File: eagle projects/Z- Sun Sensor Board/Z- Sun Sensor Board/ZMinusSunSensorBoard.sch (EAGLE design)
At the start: 53 parts, among them U2 ADS7841E_2K5, U4 LM20BIM7X_NOPB, U6 TLV9051IDCKR, U8 TLV9051IDCKR, U9 TLV9051IDCKR

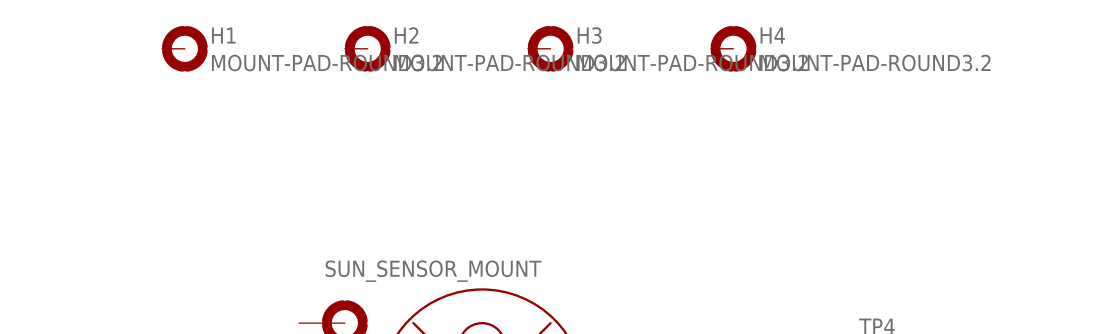
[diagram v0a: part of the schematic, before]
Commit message: Added mounting holes for sun sensor board, added standoff mounting holes to sensor board
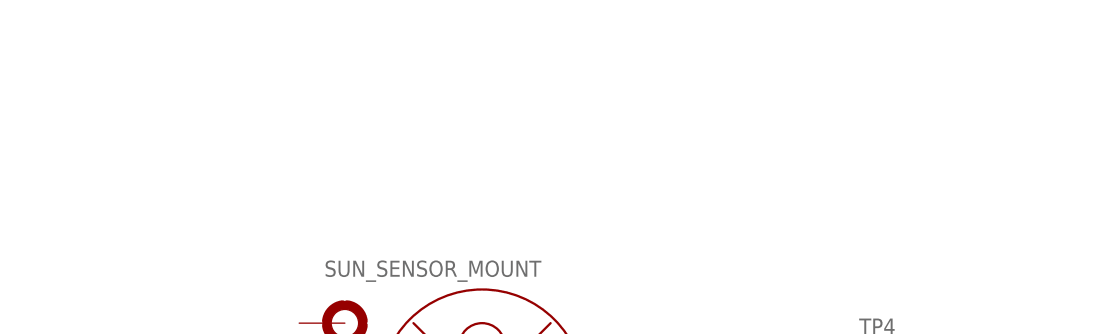
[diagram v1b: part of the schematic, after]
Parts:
- removed H1, H2, H3, H4: MOUNT-PAD-ROUND3.2, holes:MOUNT-PAD-ROUND3.2
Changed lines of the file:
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@@
 <part name="SUPPLY1" library="supply2" library_urn="urn:adsk.eagle:library:372" deviceset="GND" device=""/>
 <part name="SUPPLY2" library="supply2" library_urn="urn:adsk.eagle:library:372" deviceset="GND" device=""/>
-<part name="H1" library="holes" library_urn="urn:adsk.eagle:library:237" deviceset="MOUNT-PAD-ROUND" device="3.2" package3d_urn="urn:adsk.eagle:package:14282/1"/>
-<part name="H2" library="holes" library_urn="urn:adsk.eagle:library:237" deviceset="MOUNT-PAD-ROUND" device="3.2" package3d_urn="urn:adsk.eagle:package:14282/1"/>
-<part name="H3" library="holes" library_urn="urn:adsk.eagle:library:237" deviceset="MOUNT-PAD-ROUND" device="3.2" package3d_urn="urn:adsk.eagle:package:14282/1"/>
-<part name="H4" library="holes" library_urn="urn:adsk.eagle:library:237" deviceset="MOUNT-PAD-ROUND" device="3.2" package3d_urn="urn:adsk.eagle:package:14282/1"/>
 <part name="TP4" library="my_library" library_urn="urn:adsk.eagle:library:22876504" deviceset="TESTPOINT" device="" package3d_urn="urn:adsk.eagle:package:24605432/2"/>
 </parts>
@@
 <attribute name="VALUE" x="236.855" y="159.385" size="1.778" layer="96"/>
 </instance>
-<instance part="H1" gate="G$1" x="162.56" y="200.66" smashed="yes">
-<attribute name="NAME" x="165.354" y="201.2442" size="1.778" layer="95"/>
-<attribute name="VALUE" x="165.354" y="198.1962" size="1.778" layer="96"/>
-</instance>
-<instance part="H2" gate="G$1" x="182.88" y="200.66" smashed="yes">
-<attribute name="NAME" x="185.674" y="201.2442" size="1.778" layer="95"/>
-<attribute name="VALUE" x="185.674" y="198.1962" size="1.778" layer="96"/>
-</instance>
-<instance part="H3" gate="G$1" x="203.2" y="200.66" smashed="yes">
-<attribute name="NAME" x="205.994" y="201.2442" size="1.778" layer="95"/>
-<attribute name="VALUE" x="205.994" y="198.1962" size="1.778" layer="96"/>
-</instance>
-<instance part="H4" gate="G$1" x="223.52" y="200.66" smashed="yes">
-<attribute name="NAME" x="226.314" y="201.2442" size="1.778" layer="95"/>
-<attribute name="VALUE" x="226.314" y="198.1962" size="1.778" layer="96"/>
-</instance>
 <instance part="TP4" gate="G$1" x="238.76" y="167.64" smashed="yes">

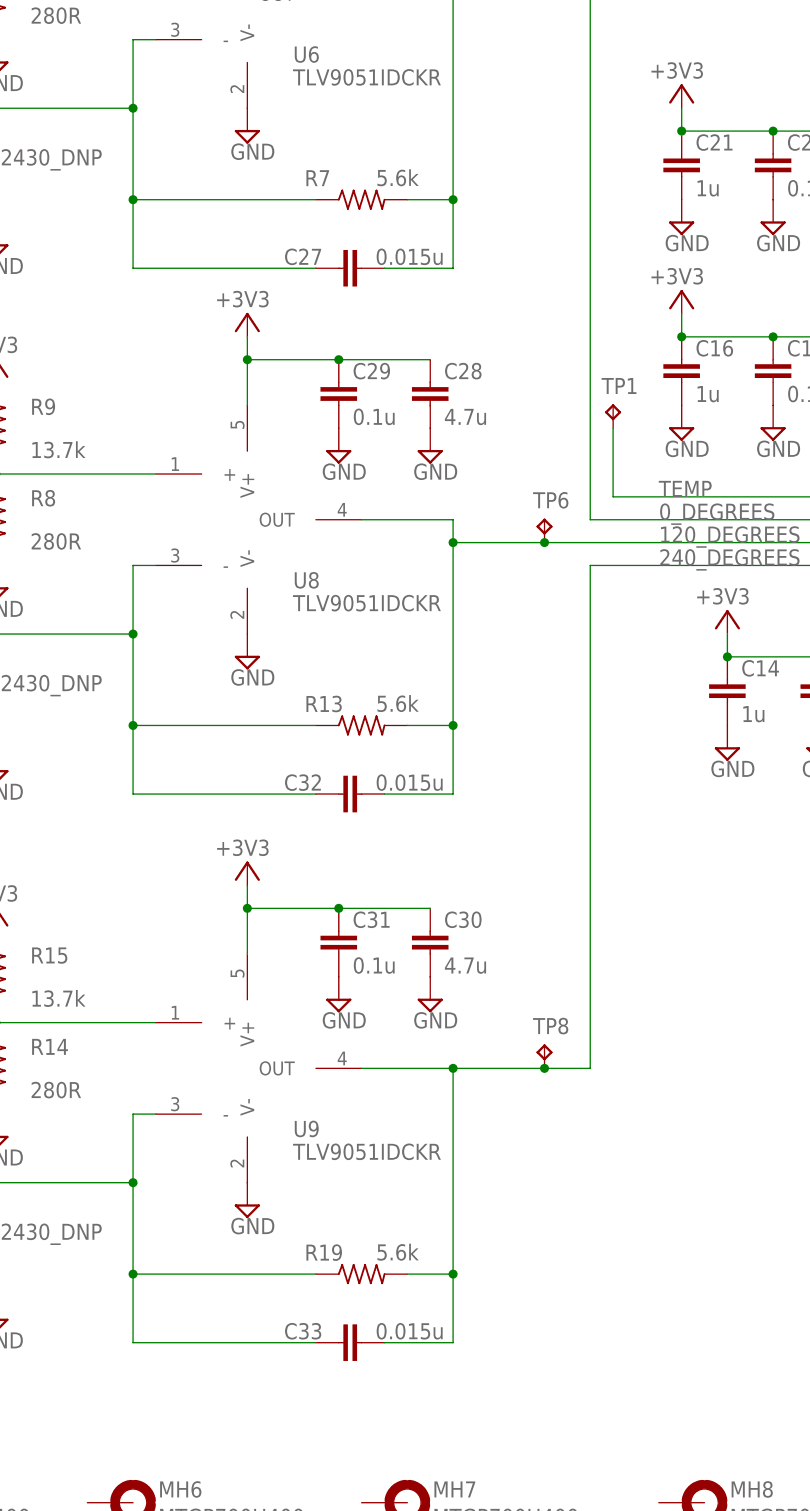
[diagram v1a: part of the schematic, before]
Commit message: Small value updates, new titleblock, and added bom
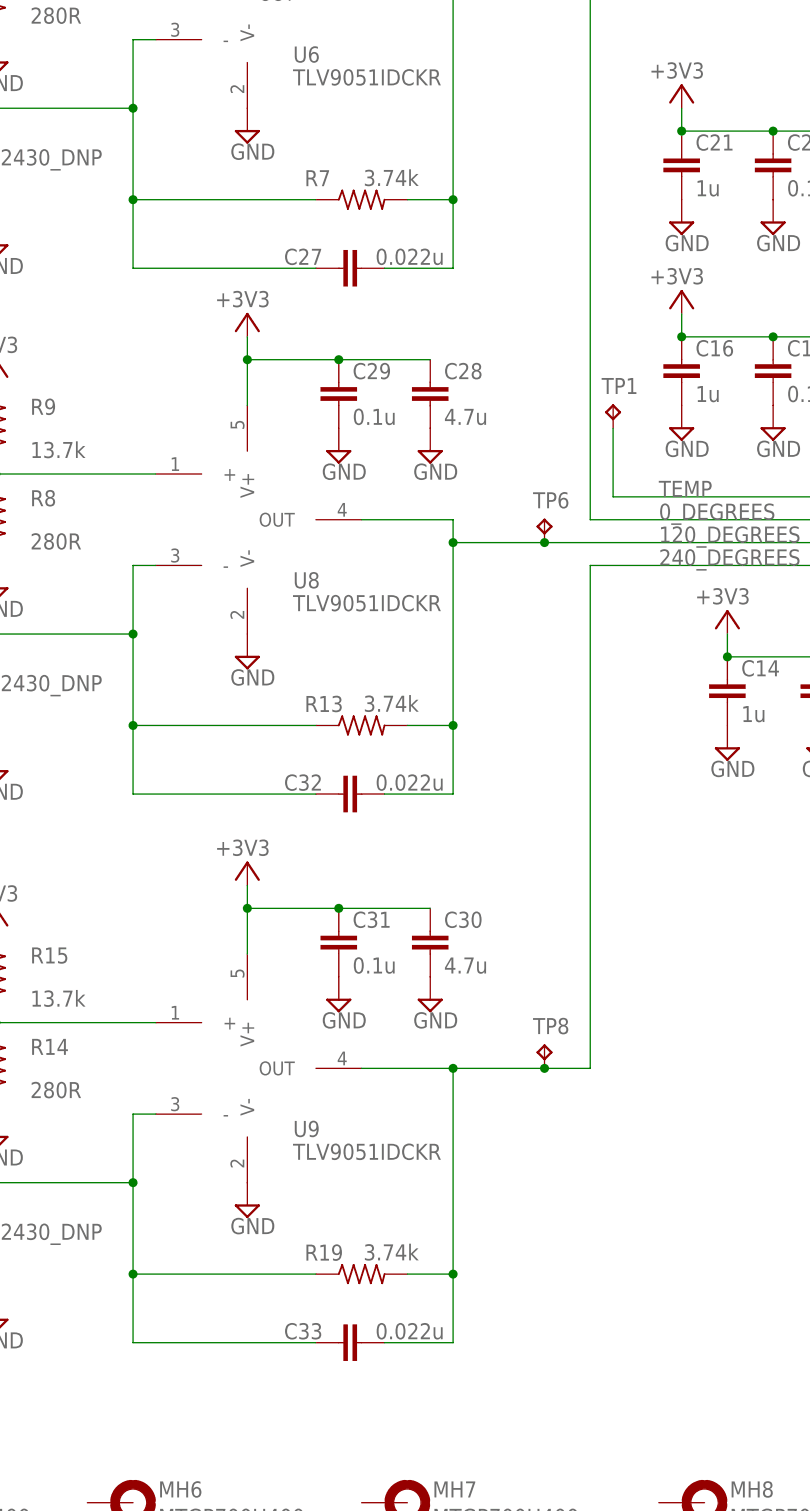
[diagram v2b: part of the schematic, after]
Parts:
- C12: device rcl:C-EUC0603 -> rcl:C-EUC0402
- C27, C32, C33: value 0.015u -> 0.022u
- R13, R19, R7: value 5.6k -> 3.74k
- R26: device rcl:R-US_R0603 -> rcl:R-US_R0402
